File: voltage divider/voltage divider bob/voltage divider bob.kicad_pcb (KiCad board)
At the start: 2 copper layers, 21.6 x 10.2 mm, 4 parts, among them con1 con_2pin, con2 3pin_connector

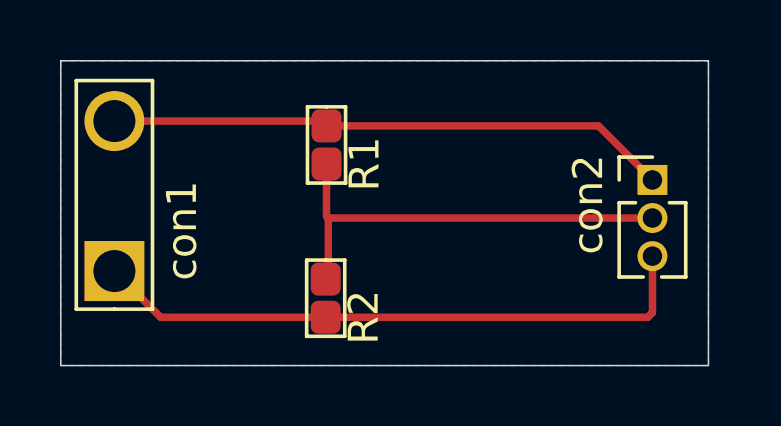
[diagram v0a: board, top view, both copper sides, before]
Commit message: silkscreen
silkscreen toegevoegd
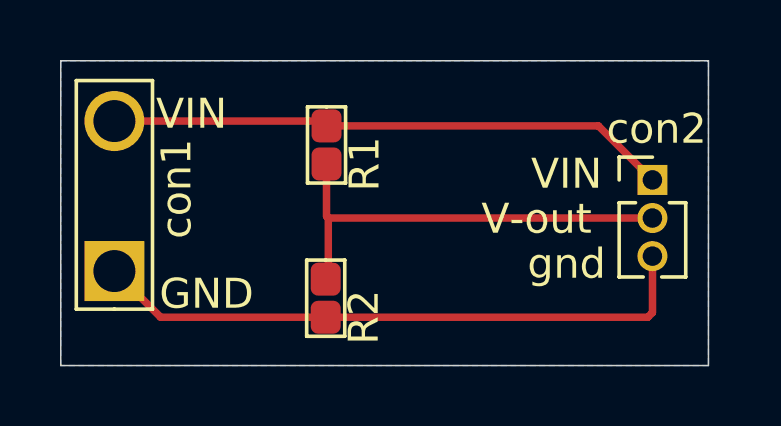
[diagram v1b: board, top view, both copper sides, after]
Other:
- board text added: "GND"
- board text added: "V-out"
- board text added: "VIN"
- board text added: "gnd"
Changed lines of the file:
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@@
   (general
     (thickness 1.6)
-    (drawings 6)
+    (drawings 11)
     (tracks 14)
     (zones 0)
@@
     (pad_to_mask_clearance 0)
     (aux_axis_origin 0 0)
-    (visible_elements FFFFFF7F)
+    (visible_elements 7FFFFFFF)
     (pcbplotparams
       (layerselection 0x010fc_ffffffff)
@@
   (module connectors_user:2pin_screw (layer F.Cu)
     (at 105.92816 69.2404 90)
-    (fp_text reference con1 (at 1.3462 2.25552 90) (layer F.SilkS)
+    (fp_text reference con1 (at 2.7404 2.07184 90) (layer F.SilkS)
       (effects (font (size 1 1) (thickness 0.15)))
     )
@@
       (effects (font (size 1 1) (thickness 0.15)))
     )
+    (fp_line (start -1.27 1.27) (end -1.27 0) (layer F.SilkS) (width 0.12))
+    (fp_line (start 6.35 1.27) (end -1.27 1.27) (layer F.SilkS) (width 0.12))
+    (fp_line (start 6.35 -1.27) (end 6.35 1.27) (layer F.SilkS) (width 0.12))
+    (fp_line (start -1.27 -1.27) (end 6.35 -1.27) (layer F.SilkS) (width 0.12))
     (fp_line (start -1.27 0) (end -1.27 -1.27) (layer F.SilkS) (width 0.12))
-    (fp_line (start -1.27 -1.27) (end 6.35 -1.27) (layer F.SilkS) (width 0.12))
-    (fp_line (start 6.35 -1.27) (end 6.35 1.27) (layer F.SilkS) (width 0.12))
-    (fp_line (start 6.35 1.27) (end -1.27 1.27) (layer F.SilkS) (width 0.12))
-    (fp_line (start -1.27 1.27) (end -1.27 0) (layer F.SilkS) (width 0.12))
     (pad 1 thru_hole rect (at 0 0 90) (size 2 2) (drill 1.4) (layers *.Cu *.Mask)
       (net 1 GND))
@@
     (descr "Through hole straight pin header, 1x03, 1.27mm pitch, single row")
     (tags "Through hole pin header THT 1x03 1.27mm single row")
-    (fp_text reference con2 (at -2.14122 0.82296 90) (layer F.SilkS)
+    (fp_text reference con2 (at 0.1369 -1.70256 180) (layer F.SilkS)
       (effects (font (size 1 1) (thickness 0.15)))
     )
@@
       (effects (font (size 1 1) (thickness 0.15)))
     )
+    (fp_line (start -0.525 -0.635) (end 1.05 -0.635) (layer F.Fab) (width 0.1))
+    (fp_line (start 1.05 -0.635) (end 1.05 3.175) (layer F.Fab) (width 0.1))
+    (fp_line (start 1.05 3.175) (end -1.05 3.175) (layer F.Fab) (width 0.1))
+    (fp_line (start -1.05 3.175) (end -1.05 -0.11) (layer F.Fab) (width 0.1))
+    (fp_line (start -1.05 -0.11) (end -0.525 -0.635) (layer F.Fab) (width 0.1))
+    (fp_line (start -1.11 3.235) (end -0.30753 3.235) (layer F.SilkS) (width 0.12))
+    (fp_line (start 0.30753 3.235) (end 1.11 3.235) (layer F.SilkS) (width 0.12))
+    (fp_line (start -1.11 0.76) (end -1.11 3.235) (layer F.SilkS) (width 0.12))
+    (fp_line (start 1.11 0.76) (end 1.11 3.235) (layer F.SilkS) (width 0.12))
+    (fp_line (start -1.11 0.76) (end -0.563471 0.76) (layer F.SilkS) (width 0.12))
+    (fp_line (start 0.563471 0.76) (end 1.11 0.76) (layer F.SilkS) (width 0.12))
+    (fp_line (start -1.11 0) (end -1.11 -0.76) (layer F.SilkS) (width 0.12))
+    (fp_line (start -1.11 -0.76) (end 0 -0.76) (layer F.SilkS) (width 0.12))
+    (fp_line (start -1.55 -1.15) (end -1.55 3.7) (layer F.CrtYd) (width 0.05))
+    (fp_line (start -1.55 3.7) (end 1.55 3.7) (layer F.CrtYd) (width 0.05))
+    (fp_line (start 1.55 3.7) (end 1.55 -1.15) (layer F.CrtYd) (width 0.05))
     (fp_line (start 1.55 -1.15) (end -1.55 -1.15) (layer F.CrtYd) (width 0.05))
-    (fp_line (start 1.55 3.7) (end 1.55 -1.15) (layer F.CrtYd) (width 0.05))
-    (fp_line (start -1.55 3.7) (end 1.55 3.7) (layer F.CrtYd) (width 0.05))
-    (fp_line (start -1.55 -1.15) (end -1.55 3.7) (layer F.CrtYd) (width 0.05))
-    (fp_line (start -1.11 -0.76) (end 0 -0.76) (layer F.SilkS) (width 0.12))
-    (fp_line (start -1.11 0) (end -1.11 -0.76) (layer F.SilkS) (width 0.12))
-    (fp_line (start 0.563471 0.76) (end 1.11 0.76) (layer F.SilkS) (width 0.12))
-    (fp_line (start -1.11 0.76) (end -0.563471 0.76) (layer F.SilkS) (width 0.12))
-    (fp_line (start 1.11 0.76) (end 1.11 3.235) (layer F.SilkS) (width 0.12))
-    (fp_line (start -1.11 0.76) (end -1.11 3.235) (layer F.SilkS) (width 0.12))
-    (fp_line (start 0.30753 3.235) (end 1.11 3.235) (layer F.SilkS) (width 0.12))
-    (fp_line (start -1.11 3.235) (end -0.30753 3.235) (layer F.SilkS) (width 0.12))
-    (fp_line (start -1.05 -0.11) (end -0.525 -0.635) (layer F.Fab) (width 0.1))
-    (fp_line (start -1.05 3.175) (end -1.05 -0.11) (layer F.Fab) (width 0.1))
-    (fp_line (start 1.05 3.175) (end -1.05 3.175) (layer F.Fab) (width 0.1))
-    (fp_line (start 1.05 -0.635) (end 1.05 3.175) (layer F.Fab) (width 0.1))
-    (fp_line (start -0.525 -0.635) (end 1.05 -0.635) (layer F.Fab) (width 0.1))
     (fp_text user %R (at 0 1.27 90) (layer F.Fab)
       (effects (font (size 1 1) (thickness 0.15)))
@@
       (effects (font (size 1 1) (thickness 0.15)))
     )
+    (fp_line (start -0.635 0) (end -0.635 -0.635) (layer F.SilkS) (width 0.12))
+    (fp_line (start -0.635 -0.635) (end 1.905 -0.635) (layer F.SilkS) (width 0.12))
+    (fp_line (start 1.905 -0.635) (end 1.905 0.635) (layer F.SilkS) (width 0.12))
+    (fp_line (start 1.905 0.635) (end -0.635 0.635) (layer F.SilkS) (width 0.12))
     (fp_line (start -0.635 0.635) (end -0.635 0) (layer F.SilkS) (width 0.12))
-    (fp_line (start 1.905 0.635) (end -0.635 0.635) (layer F.SilkS) (width 0.12))
-    (fp_line (start 1.905 -0.635) (end 1.905 0.635) (layer F.SilkS) (width 0.12))
-    (fp_line (start -0.635 -0.635) (end 1.905 -0.635) (layer F.SilkS) (width 0.12))
-    (fp_line (start -0.635 0) (end -0.635 -0.635) (layer F.SilkS) (width 0.12))
     (pad 1 smd roundrect (at 0 0) (size 1 1.1) (layers F.Cu F.Paste F.Mask) (roundrect_rratio 0.25)
       (net 2 "Net-(R1-Pad1)"))
@@
       (effects (font (size 1 1) (thickness 0.15)))
     )
+    (fp_line (start -0.635 0.635) (end -0.635 0) (layer F.SilkS) (width 0.12))
+    (fp_line (start 1.905 0.635) (end -0.635 0.635) (layer F.SilkS) (width 0.12))
+    (fp_line (start 1.905 -0.635) (end 1.905 0.635) (layer F.SilkS) (width 0.12))
+    (fp_line (start -0.635 -0.635) (end 1.905 -0.635) (layer F.SilkS) (width 0.12))
     (fp_line (start -0.635 0) (end -0.635 -0.635) (layer F.SilkS) (width 0.12))
-    (fp_line (start -0.635 -0.635) (end 1.905 -0.635) (layer F.SilkS) (width 0.12))
-    (fp_line (start 1.905 -0.635) (end 1.905 0.635) (layer F.SilkS) (width 0.12))
-    (fp_line (start 1.905 0.635) (end -0.635 0.635) (layer F.SilkS) (width 0.12))
-    (fp_line (start -0.635 0.635) (end -0.635 0) (layer F.SilkS) (width 0.12))
     (pad 2 smd roundrect (at 1.27 0) (size 1 1.1) (layers F.Cu F.Paste F.Mask) (roundrect_rratio 0.25)
       (net 1 GND))
@@
     )
   )
+  (gr_text "GND\n" (at 109 70) (layer F.SilkS)
+    (effects (font (size 1 1) (thickness 0.15)))
+  )
+  (gr_text "VIN\n" (at 108.5 64) (layer F.SilkS)
+    (effects (font (size 1 1) (thickness 0.15)))
+  )
+  (gr_text "VIN\n" (at 121 66) (layer F.SilkS)
+    (effects (font (size 1 1) (thickness 0.15)))
+  )
+  (gr_text "V-out\n" (at 120 67.5) (layer F.SilkS)
+    (effects (font (size 1 1) (thickness 0.15)))
+  )
+  (gr_text "gnd\n" (at 121 69) (layer F.SilkS)
+    (effects (font (size 1 1) (thickness 0.15)))
+  )
   (dimension 10.16 (width 0.15) (layer Cmts.User)
